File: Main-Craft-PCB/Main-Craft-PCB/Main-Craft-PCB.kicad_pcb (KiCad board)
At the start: 2 copper layers, 218 parts, among them J1 UART_1, J10 S500_2, J11 S500_3, J12 S500_4, J13 SOL_1, J14 SOL_2, J15 RELAY_1, J16 RELAY_2, J17 RELAY_3, J18 RELAY_3, J19 SOL_3, J2 UART_2, J20 SOL_4, J21 PWR_IN, J22 Conn_01x10, J23 BAT_IN, J24 VESC_1, J25 VESC_2, J26 VESC_3, J27 VESC_4, J3 UART_3, J4 UART_4, J5 LEDS, J6 LEDS, J7 LEDS, J8 LEDS, J9 S500_1, Q1 TIP120, Q10 S9013, Q11 S9013, Q12 S9013, Q13 S9013, Q14 S9013, Q15 IRFR9014PBF, Q16 S9013, Q2 TIP120, Q3 TIP120, Q4 TIP120, Q5 S9013, Q6 S9013, Q7 S9013, Q8 S9013, Q9 S9013, U1 NUCLEO144-F429ZI, U10 ZSR330GTA, U11 ZLDO1117G50TA, U12 BFU590GX, U2 Pi Pico, U3 ESP8266, U4 SN74LV4052, U5 LM358DR2G, U6 LM358DR2G, U7 LM358DR2G, U8 74HC14, U9 74HC14

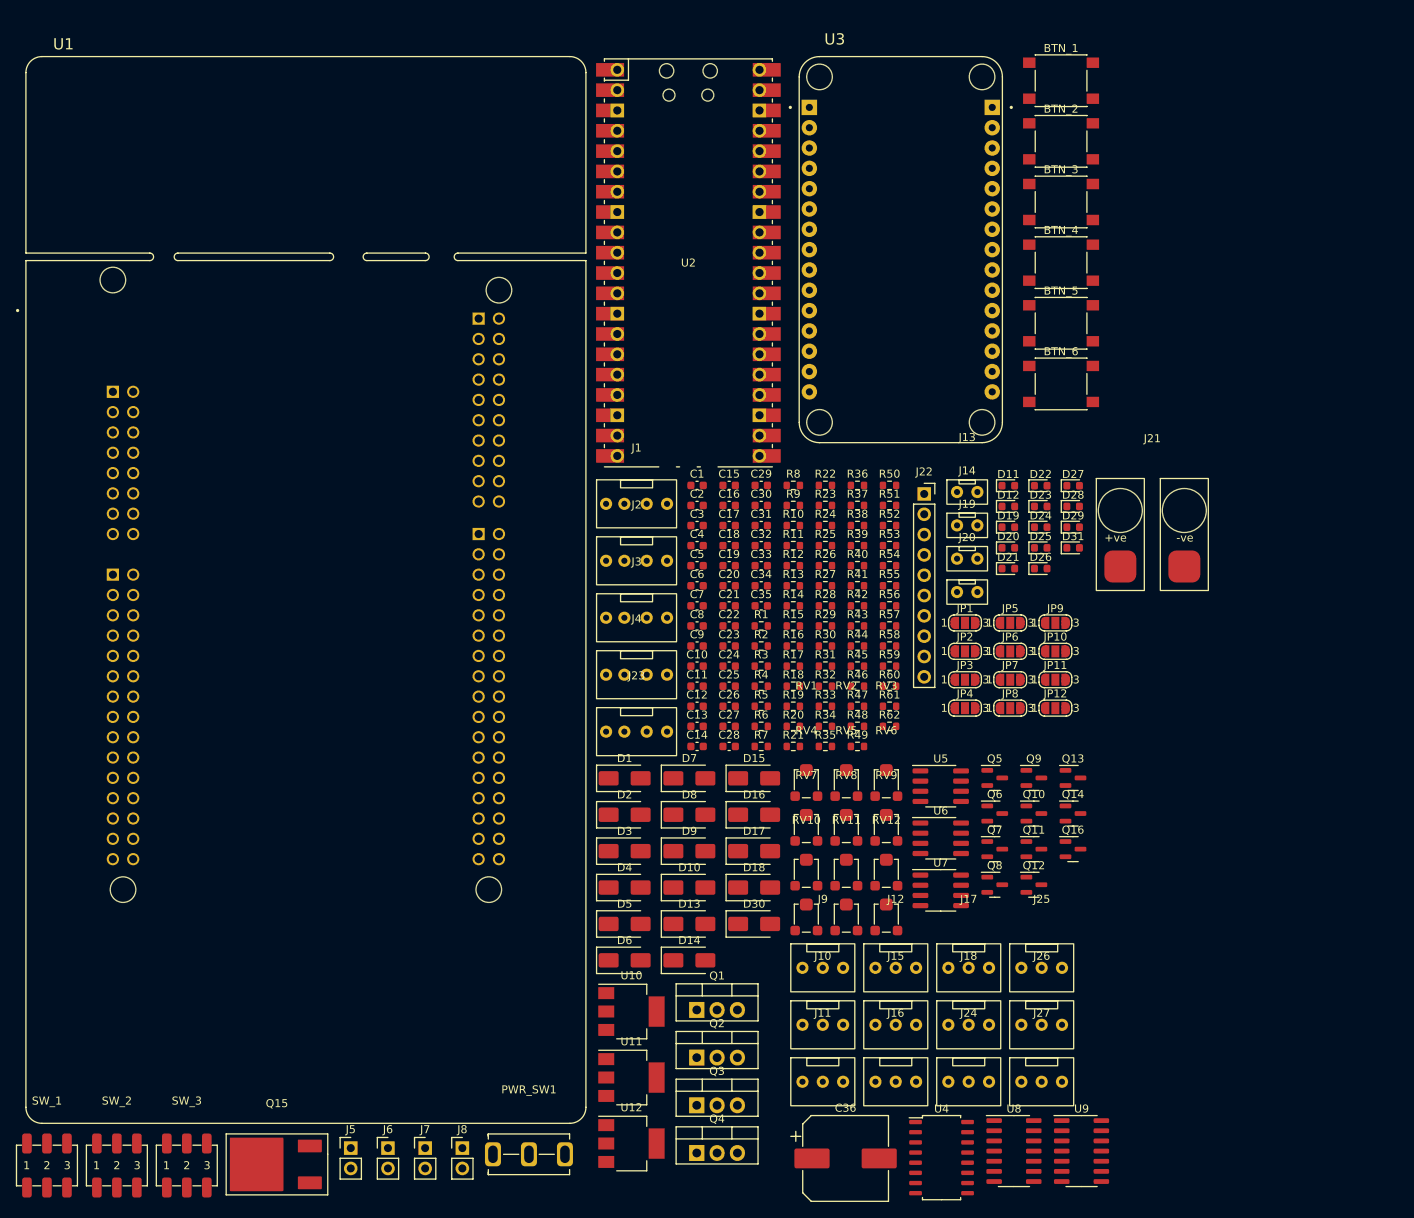
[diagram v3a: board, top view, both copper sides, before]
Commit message: finish component placement and start traces
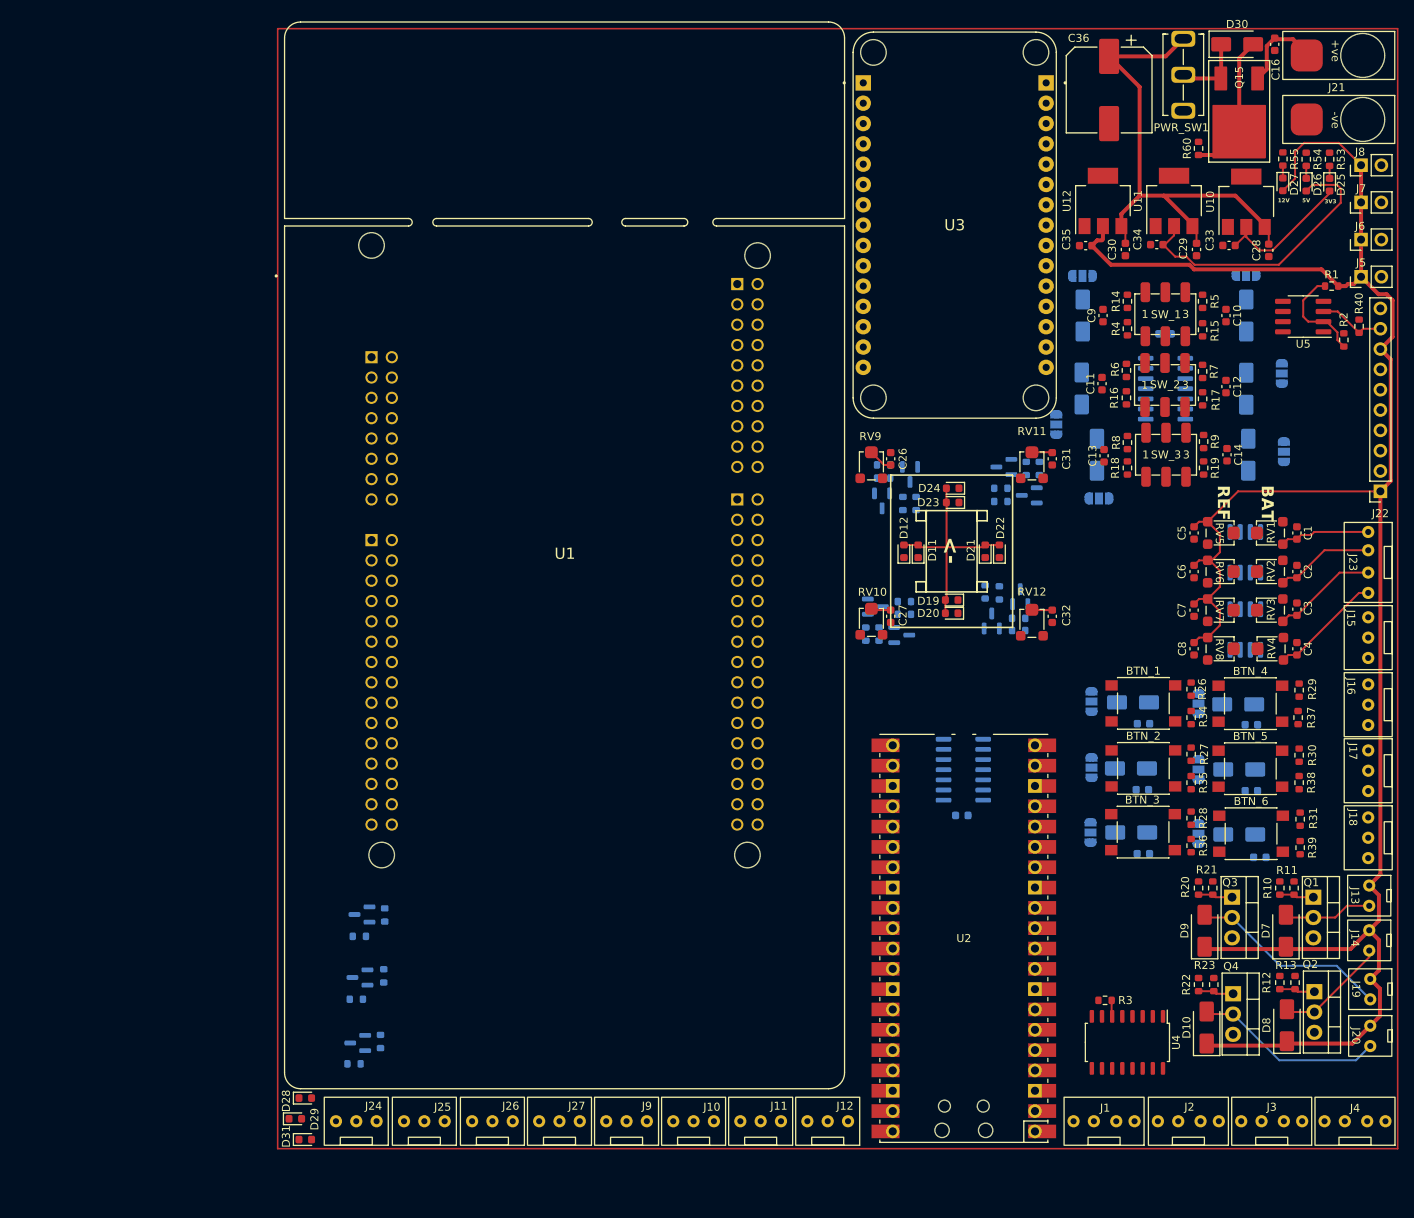
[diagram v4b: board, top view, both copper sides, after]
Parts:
- removed C24, C25: 100nF, Capacitor_SMD:C_0603_1608Metric
- C15, C17, C18, C19, C20, C21, C22, C23, D1, D13, D14, D15, D16, D17, D18, D2, D3, D4, D5, D6, JP1, JP10, JP11, JP12, JP2, JP3, JP4, JP5, JP6, JP7, JP8, JP9, Q10, Q11, Q12, Q13, Q14, Q16, Q5, Q6, Q7, Q8, Q9, R24, R25, R32, R33, R41, R42, R43, R44, R45, R46, R47, R48, R49, R50, R51, R52, R56, R57, R58, R59, R61, R62, U6, U7, U8, U9: moved to B.Cu
- moved Q15 178.2 mm to (184.4, 31.8), turned to 90 degrees
- moved SW_1 175.7 mm to (175.2, 54.6)
- moved J5 166.8 mm to (199.6, 49.9), turned to 90 degrees
- moved J8 166.5 mm to (199.6, 35.9), turned to 90 degrees
- moved J6 166.4 mm to (199.6, 45.2), turned to 90 degrees
- moved J7 166.3 mm to (199.6, 40.6), turned to 90 degrees
- moved SW_2 163.4 mm to (175.1, 63.4)
- moved PWR_SW1 157.8 mm to (177.4, 24.6), turned to -90 degrees
- moved SW_3 151.2 mm to (175.3, 72.1)
- moved C36 137.6 mm to (168.1, 26.5), turned to -90 degrees
- moved U12 131.7 mm to (167.4, 40.4), turned to 90 degrees
- moved U11 128.9 mm to (176.3, 40.4), turned to 90 degrees
- moved U10 127.1 mm to (185.3, 40.5), turned to 90 degrees
- moved D30 125.4 mm to (184.2, 20.8)
- moved D29 122.2 mm to (66.4, 155.1)
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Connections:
- J22 pad 1: VIN -> +12V
- J23 pad 1: BATT_1_IN -> BATT_4_IN
- J23 pad 2: BATT_2_IN -> BATT_3_IN
- J23 pad 3: BATT_3_IN -> BATT_2_IN
- J23 pad 4: BATT_4_IN -> BATT_1_IN
- J24 pad 1: VESC_IN_5V -> VESC_1
- J24 pad 2: VESC_1 -> unconnected-(J24-Pin_2-Pad2)
- J25 pad 1: VESC_IN_5V -> VESC_2
- J25 pad 2: VESC_2 -> unconnected-(J25-Pin_2-Pad2)
- J26 pad 1: VESC_IN_5V -> VESC_3
- J26 pad 2: VESC_3 -> unconnected-(J26-Pin_2-Pad2)
- J27 pad 1: VESC_IN_5V -> VESC_4
- J27 pad 2: VESC_4 -> unconnected-(J27-Pin_2-Pad2)
- R26 pad 2: +5V -> +3V3
- R27 pad 2: +5V -> +3V3
- R28 pad 2: +5V -> +3V3
- R29 pad 2: +5V -> +3V3
- R30 pad 2: +5V -> +3V3
- R31 pad 2: +5V -> +3V3
- R4 pad 2: +5V -> +3V3
- R5 pad 2: +5V -> +3V3
- R6 pad 2: +5V -> +3V3
- R7 pad 2: +5V -> +3V3
- R8 pad 2: +5V -> +3V3
- R9 pad 2: +5V -> +3V3
- U4 pad 4: /Y4 -> /Y3
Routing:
- net +12V: track 0.00 -> 264.3 mm
- net +5V: track 0.00 -> 64.0 mm
- net VIN: track 0.00 -> 63.7 mm
- net Net-(D9-A): track 0.00 -> 25.1 mm
- net Net-(D10-A): track 0.00 -> 23.7 mm
- net +3V3: track 0.00 -> 18.5 mm
- net Net-(D30-A): track 0.00 -> 17.9 mm
- net Net-(D8-A): track 0.00 -> 14.1 mm
- net BATT_1_IN: track 0.00 -> 14.1 mm
- net BATT_2_IN: track 0.00 -> 13.2 mm
- net Net-(U5A--): track 0.00 -> 12.7 mm
- net BATT_3_IN: track 0.00 -> 12.4 mm
- net BATT_4_IN: track 0.00 -> 11.3 mm
- net Net-(D7-A): track 0.00 -> 11.2 mm
- net 12V_INPUT: track 0.00 -> 11.0 mm
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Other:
- board text added: "->"
- board text added: "12V"
- board text added: "3V3"
- board text added: "5V"
- board text added: "BAT"
- board text added: "REF"

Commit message: Finish PCB ready for checking
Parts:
- U1: footprint My_library:MODULE_NUCLEO-F429ZI -> My_library:MODULE_NUCLEO-F429ZI_JUST_PINS; moved to B.Cu
- moved J12 25.1 mm to (107.8, 155.4)
- moved J9 25.1 mm to (133.0, 155.4)
- moved Q14 8.20 mm to (74.4, 137.8)
- moved R58 8.20 mm to (77.3, 137.9)
- moved R59 8.20 mm to (74.1, 140.5)
- moved R62 7.75 mm to (74.3, 132.5)
- moved Q16 7.75 mm to (74.8, 129.7)
- moved R61 7.75 mm to (77.8, 129.5)
- moved PWR_SW1 1.96 mm to (177.5, 26.6)
- moved R60 1.11 mm to (178.8, 34.8), turned to 180 degrees
- turned U1 to 180 degrees
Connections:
- J22 pad 2: MOSI_1 -> CLK_1
- J22 pad 3: MISO_1 -> MOSI_1
- J22 pad 4: CLK_1 -> MISO_1
- U1 pad 38: BTN_1 -> BTN_2
- U1 pad 40: BTN_6 -> BTN_4
- U1 pad 41: BTN_4 -> BTN_6
- U1 pad 45: BTN_2 -> BTN_1
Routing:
- net +3V3: track 18.5 -> 483.6 mm, vias 0 -> 14
- net +5V: track 64.0 -> 443.8 mm, vias 0 -> 8
- net LOW_VOLT_4: track 0.00 -> 145.8 mm, vias 0 -> 6
- net SOL_2: track 0.00 -> 141.3 mm
- net LOW_VOLT_3: track 0.00 -> 139.9 mm, vias 0 -> 3
- net SOL_4: track 0.00 -> 129.3 mm
- net SOL_1: track 0.00 -> 128.6 mm
- net LOW_VOLT_2: track 0.00 -> 118.9 mm, vias 0 -> 5
- net LOW_VOLT_1: track 0.00 -> 118.7 mm, vias 0 -> 3
- net VESC_2: track 0.00 -> 114.7 mm, vias 0 -> 8
- net RELAY_1: track 0.00 -> 114.2 mm, vias 0 -> 3
- net SOL_3: track 0.00 -> 113.7 mm
- net S500_1: track 0.00 -> 111.1 mm, vias 0 -> 1
- net MISO_1: track 0.00 -> 109.0 mm
- net VESC_3: track 0.00 -> 108.2 mm, vias 0 -> 8
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- added copper zone on B.Cu, net Earth
- added copper zone on F.Cu, net Earth
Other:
- board outline added: 140.5 x 139.8 mm

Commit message: Add final touches to PCB
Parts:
- Q10, Q11, Q12, Q13, Q14, Q16, Q5, Q6, Q7, Q8, Q9: value S9013 -> BC817
- U1: footprint My_library:MODULE_NUCLEO-F429ZI_JUST_PINS -> My_library:MODULE_NUCLEO-F429ZI
- moved Q5 0.26 mm to (143.3, 74.9)
- moved J21 0.25 mm to (196.8, 26.5)
- moved Q11 0.25 mm to (158.4, 77.2)
- moved Q9 0.23 mm to (153.4, 93.1)
- moved Q10 0.13 mm to (157.0, 89.7)
- moved Q7 0.11 mm to (139.0, 91.2)
- moved Q8 0.11 mm to (142.3, 94.7)
- moved Q14 0.10 mm to (74.5, 137.9)
- moved Q12 0.08 mm to (155.0, 73.6)
- moved Q13 0.07 mm to (74.2, 145.7)
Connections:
- Q10 pad 1: Earth -> Net-(Q10-B)
- Q10 pad 2: Net-(Q10-B) -> Earth
- Q11 pad 1: Earth -> Net-(Q11-B)
- Q11 pad 2: Net-(Q11-B) -> Earth
- Q12 pad 1: Earth -> Net-(Q12-B)
- Q12 pad 2: Net-(Q12-B) -> Earth
- Q13 pad 1: Earth -> Net-(Q13-B)
- Q13 pad 2: Net-(Q13-B) -> Earth
- Q14 pad 1: Earth -> Net-(Q14-B)
- Q14 pad 2: Net-(Q14-B) -> Earth
- Q16 pad 1: Earth -> Net-(Q16-B)
- Q16 pad 2: Net-(Q16-B) -> Earth
- Q5 pad 1: Earth -> Net-(Q5-B)
- Q5 pad 2: Net-(Q5-B) -> Earth
- Q6 pad 1: Earth -> Net-(Q6-B)
- Q6 pad 2: Net-(Q6-B) -> Earth
- Q7 pad 1: Earth -> Net-(Q7-B)
- Q7 pad 2: Net-(Q7-B) -> Earth
- Q8 pad 1: Earth -> Net-(Q8-B)
- Q8 pad 2: Net-(Q8-B) -> Earth
- Q9 pad 1: Earth -> Net-(Q9-B)
- Q9 pad 2: Net-(Q9-B) -> Earth
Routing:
- net Earth: track 57.8 -> 77.0 mm, vias 143 -> 144
- net Net-(Q11-B): track 5.80 -> 1.62 mm
- net Net-(Q12-B): track 1.88 -> 5.43 mm
- net Net-(Q7-B): track 4.61 -> 1.74 mm
- net Net-(Q5-B): track 4.67 -> 1.80 mm
- net Net-(Q9-B): track 4.26 -> 1.66 mm
- net Net-(Q12-C): track 3.23 -> 4.30 mm
- net Net-(Q10-B): track 1.81 -> 2.76 mm
- net Net-(Q8-B): track 1.91 -> 2.81 mm
- net Net-(Q6-B): track 1.93 -> 2.75 mm
- net Net-(Q14-B): track 1.93 -> 2.65 mm
- net SENS_4: track 95.9 -> 96.5 mm
- net Net-(Q16-B): track 2.17 -> 2.72 mm

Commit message: update gerbers
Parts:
- moved Q14 0.08 mm to (74.4, 137.9)
- moved R25 0.06 mm to (140.0, 75.1)
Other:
- board text added: "HEVCS Main Board Daniel Cole, Jack Pendlebury, Luke Waller, Noah Harvey"
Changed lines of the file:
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@@
   )
   (footprint "Package_TO_SOT_SMD:SOT-23" (layer "B.Cu")
-    (at 74.5005 137.856 180)
+    (at 74.422 137.856 180)
     (descr "SOT, 3 Pin (https://www.jedec.org/system/files/docs/to-236h.pdf variant AB), generated with kicad-footprint-generator ipc_gullwing_generator.py")
     (tags "SOT TO_SOT_SMD")
@@
     (property "ki_keywords" "NPN Transistor")
     (attr smd)
-    (fp_text reference "Q5" (at 0 2.4 90) (layer "B.SilkS")
+    (fp_text reference "Q5" (at -2.9695 -0.315 90) (layer "B.SilkS")
         (effects (font (size 1 1) (thickness 0.15)) (justify mirror))
     )
@@
   )
   (footprint "Resistor_SMD:R_0603_1608Metric" (layer "B.Cu")
-    (at 139.954 75.057 180)
+    (at 140.018 75.057 180)
     (descr "Resistor SMD 0603 (1608 Metric), square (rectangular) end terminal, IPC_7351 nominal, (Body size source: IPC-SM-782 page 72, https://www.pcb-3d.com/wordpress/wp-content/uploads/ipc-sm-782a_amendment_1_and_2.pdf), generated with kicad-footprint-generator")
     (tags "resistor")
@@
     (effects (font (size 0.8 0.8) (thickness 0.125) bold) (justify left bottom))
   )
+  (gr_text "HEVCS Main Board\nDaniel Cole, Jack Pendlebury, Luke Waller, Noah Harvey" (at 65.024 23.876) (layer "F.SilkS")
+    (effects (font (size 1.5 1.5) (thickness 0.3) bold) (justify left bottom))
+  )
   (gr_text "REF" (at 181.558 75.943 -90) (layer "F.SilkS")
     (effects (font (size 1.5 1.5) (thickness 0.3) bold) (justify left bottom))
@@
   (segment (start 77.217396 132.08) (end 78.994 132.08) (width 0.25) (layer "B.Cu") (net 1))
   (segment (start 141.286 93.727) (end 141.287 93.726) (width 0.25) (layer "B.Cu") (net 1))
-  (segment (start 137.985 90.17) (end 137.541 90.17) (width 0.25) (layer "B.Cu") (net 1))
   (segment (start 159.832 78.166) (end 159.101 78.166) (width 0.25) (layer "B.Cu") (net 1))
   (segment (start 184.023 60.071) (end 187.452 60.071) (width 0.25) (layer "B.Cu") (net 1))
@@
   (segment (start 73.279 147.927928) (end 72.936928 148.27) (width 0.25) (layer "B.Cu") (net 108))
   (segment (start 75.438 136.906) (end 77.213 138.681) (width 0.25) (layer "B.Cu") (net 109))
-  (segment (start 77.2005 138.745) (end 77.2645 138.681) (width 0.25) (layer "B.Cu") (net 109))
-  (segment (start 77.213 138.681) (end 77.2645 138.681) (width 0.25) (layer "B.Cu") (net 109))
   (segment (start 73.4845 137.795) (end 73.4845 140.303) (width 0.25) (layer "B.Cu") (net 110))
   (segment (start 73.4845 140.303) (end 73.2645 140.523) (width 0.25) (layer "B.Cu") (net 110))
@@
   (segment (start 157.024251 73.026) (end 157.7825 73.026) (width 0.25) (layer "B.Cu") (net 126))
   (segment (start 154.826749 73.025) (end 155.141749 73.34) (width 0.25) (layer "B.Cu") (net 126))
-  (segment (start 77.063928 144.651) (end 77.063928 140.817928) (width 0.25) (layer "B.Cu") (net 127))
+  (segment (start 74.549 138.200751) (end 74.549 137.504751) (width 0.25) (layer "B.Cu") (net 127))
+  (segment (start 74.041698 136.997449) (end 69.551144 136.997449) (width 0.25) (layer "B.Cu") (net 127))
   (segment (start 68.998 115.152) (end 75.946 108.204) (width 0.25) (layer "B.Cu") (net 127))
-  (segment (start 74.547 137.448249) (end 74.041698 136.942947) (width 0.25) (layer "B.Cu") (net 127))
-  (segment (start 75.616 139.37) (end 74.575249 139.37) (width 0.25) (layer "B.Cu") (net 127))
-  (segment (start 74.041 138.835751) (end 74.041 138.647751) (width 0.25) (layer "B.Cu") (net 127))
+  (segment (start 74.295 139.192) (end 74.295 138.454751) (width 0.25) (layer "B.Cu") (net 127))
+  (segment (start 77.063928 140.817928) (end 75.677 139.431) (width 0.25) (layer "B.Cu") (net 127))
+  (segment (start 74.549 137.504751) (end 74.041698 136.997449) (width 0.25) (layer "B.Cu") (net 127))
+  (segment (start 74.534 139.431) (end 74.295 139.192) (width 0.25) (layer "B.Cu") (net 127))
   (segment (start 68.998 136.444305) (end 68.998 115.152) (width 0.25) (layer "B.Cu") (net 127))
-  (segment (start 69.496642 136.942947) (end 68.998 136.444305) (width 0.25) (layer "B.Cu") (net 127))
-  (segment (start 74.041 138.647751) (end 74.547 138.141751) (width 0.25) (layer "B.Cu") (net 127))
-  (segment (start 74.575249 139.37) (end 74.041 138.835751) (width 0.25) (layer "B.Cu") (net 127))
-  (segment (start 74.547 138.141751) (end 74.547 137.448249) (width 0.25) (layer "B.Cu") (net 127))
-  (segment (start 77.063928 140.817928) (end 75.616 139.37) (width 0.25) (layer "B.Cu") (net 127))
-  (segment (start 74.041698 136.942947) (end 69.496642 136.942947) (width 0.25) (layer "B.Cu") (net 127))
-  (segment (start 74.422 130.787715) (end 74.422 130.571787) (width 0.25) (layer "B.Cu") (net 128))
-  (segment (start 77.2645 137.031) (end 77.2645 132.7635) (width 0.25) (layer "B.Cu") (net 128))
+  (segment (start 75.677 139.431) (end 74.534 139.431) (width 0.25) (layer "B.Cu") (net 127))
+  (segment (start 77.063928 144.651) (end 77.063928 140.817928) (width 0.25) (layer "B.Cu") (net 127))
+  (segment (start 69.551144 136.997449) (end 68.998 136.444305) (width 0.25) (layer "B.Cu") (net 127))
+  (segment (start 74.295 138.454751) (end 74.549 138.200751) (width 0.25) (layer "B.Cu") (net 127))
   (segment (start 72.39 126.862213) (end 72.39 114.3) (width 0.25) (layer "B.Cu") (net 128))
-  (segment (start 74.914036 129.386249) (end 72.39 126.862213) (width 0.25) (layer "B.Cu") (net 128))
   (segment (start 74.942285 131.308) (end 74.422 130.787715) (width 0.25) (layer "B.Cu") (net 128))
   (segment (start 75.809 131.308) (end 74.942285 131.308) (width 0.25) (layer "B.Cu") (net 128))
-  (segment (start 74.422 130.571787) (end 74.914036 130.079751) (width 0.25) (layer "B.Cu") (net 128))
-  (segment (start 74.914036 130.079751) (end 74.914036 129.386249) (width 0.25) (layer "B.Cu") (net 128))
+  (segment (start 74.422 130.538749) (end 74.880998 130.079751) (width 0.25) (layer "B.Cu") (net 128))
+  (segment (start 74.422 130.787715) (end 74.422 130.538749) (width 0.25) (layer "B.Cu") (net 128))
+  (segment (start 77.2645 137.031) (end 77.2645 132.7635) (width 0.25) (layer "B.Cu") (net 128))
   (segment (start 77.2645 132.7635) (end 75.809 131.308) (width 0.25) (layer "B.Cu") (net 128))
+  (segment (start 74.914036 130.079751) (end 74.914036 129.386249) (width 0.25) (layer "B.Cu") (net 128))
   (segment (start 72.39 114.3) (end 75.946 110.744) (width 0.25) (layer "B.Cu") (net 128))
+  (segment (start 74.914036 129.386249) (end 72.39 126.862213) (width 0.25) (layer "B.Cu") (net 128))
+  (segment (start 74.880998 130.079751) (end 74.914036 130.079751) (width 0.25) (layer "B.Cu") (net 128))
   (segment (start 77.763464 128.705) (end 72.898 123.839536) (width 0.25) (layer "B.Cu") (net 129))
   (segment (start 72.898 123.839536) (end 72.898 116.332) (width 0.25) (layer "B.Cu") (net 129))
